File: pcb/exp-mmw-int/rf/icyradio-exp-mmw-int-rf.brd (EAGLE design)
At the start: 85.7 x 98.4 mm, 68 parts, among them U1 ADMV1013, U2 ADMV1014

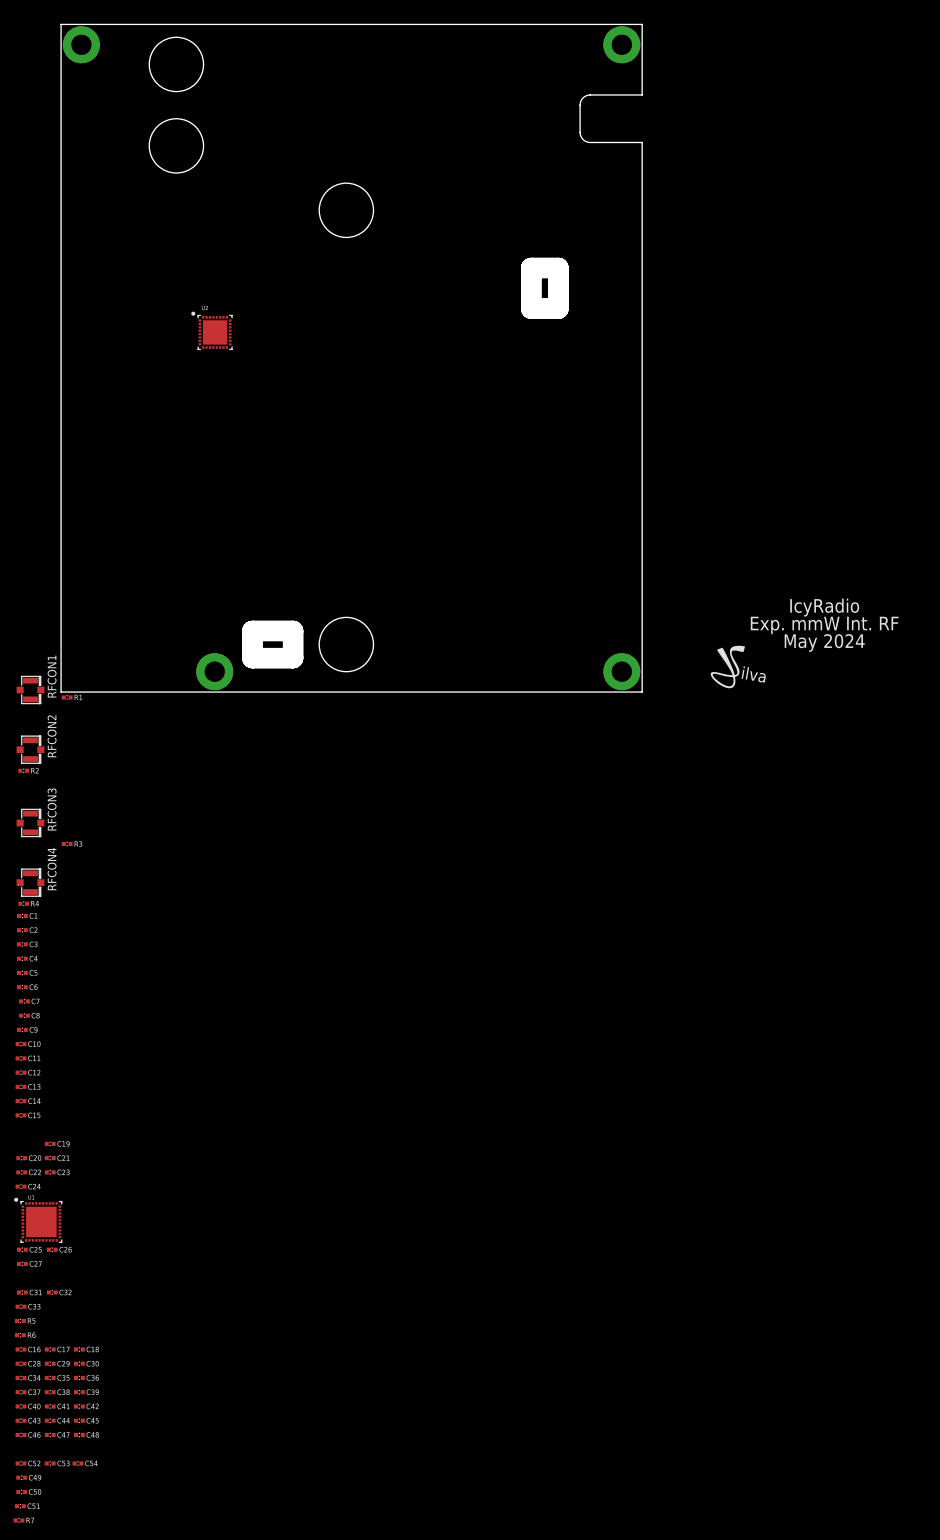
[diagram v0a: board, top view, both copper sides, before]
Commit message: pcb: Finish mmWave integrated expansion PCBs for production
Signed-off-by: João Silva <jgc3silva@gmail.com>
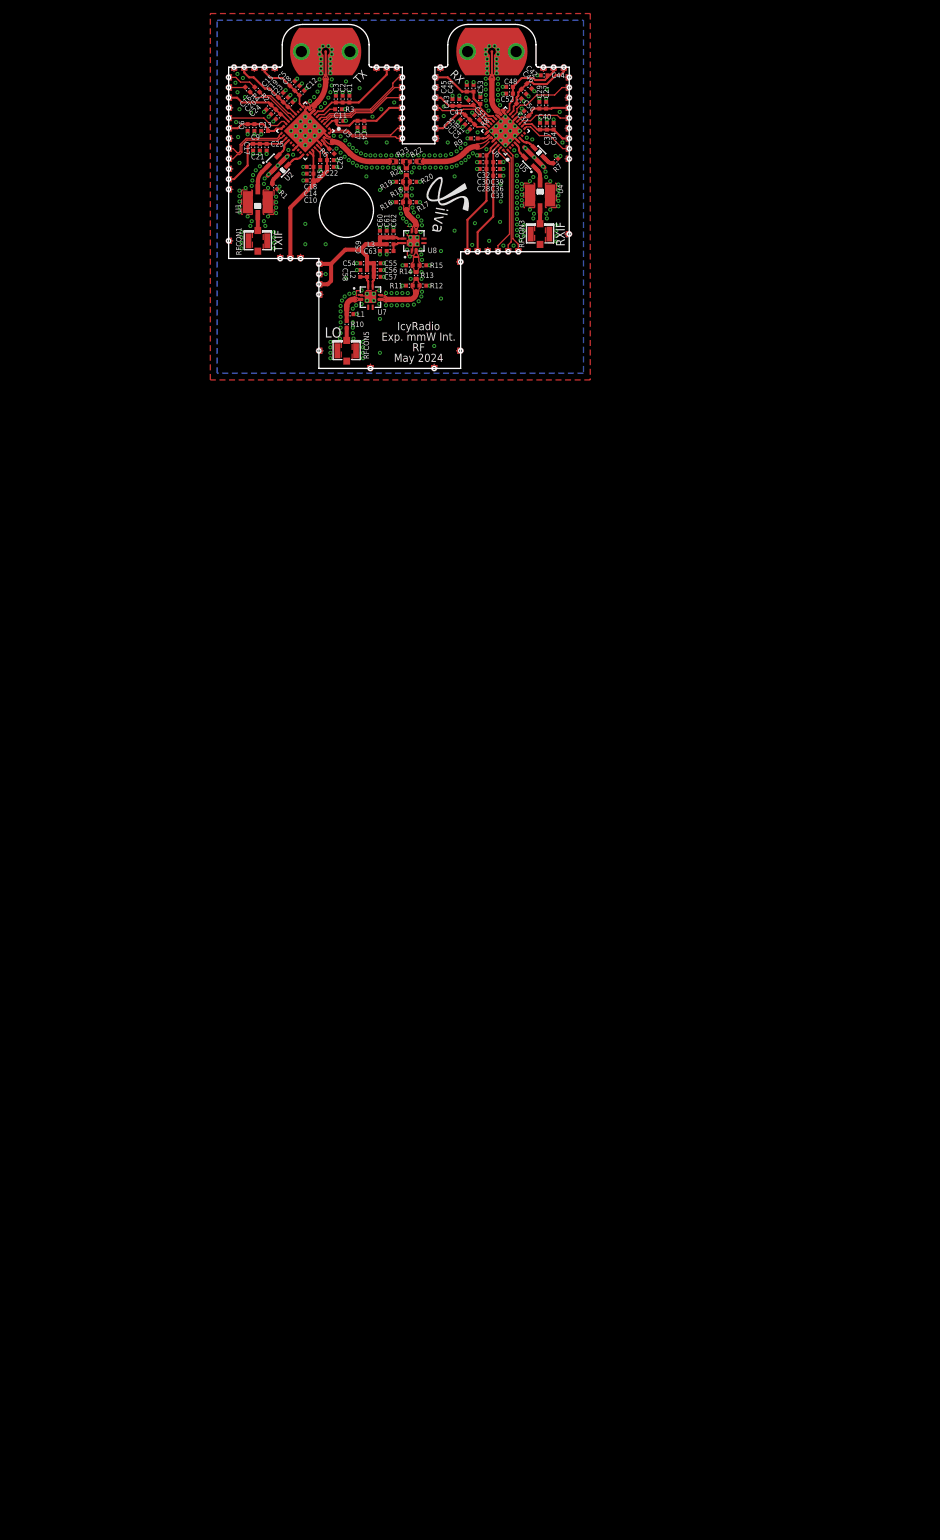
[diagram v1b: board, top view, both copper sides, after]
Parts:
- added C55, C60: 5.6pF, Capacitor:CAP0402
- added C56, C61: 18pF, Capacitor:CAP0402
- added C57, C62: 1nF, Capacitor:CAP0402
- added C58, C63: 100nF, Capacitor:CAP0402
- added C59: 10uF, Capacitor:CAP0402
- added L1: DNP, Inductor:IND0402
- added L2, L3: 3.3nH, Inductor:IND0402
- added P1, P10, P2, P22, P23, P24, P25, P26, P27, P28, P29, P3, P33, P34, P35, P36, P37, P38, P39, P4, P5, P52, P53, P54, P55, P56, P57, P58, P59, P6, P60, P64, P65, P7, P8, P9: CHOLE-0.9MM-SS, PADs:CAST_HOLE_0P9MM_SS
- added P11, P12, P13, P14, P15, P16, P17, P18, P19, P20, P21, P30, P31, P32, P40, P41, P42, P43, P44, P45, P46, P47, P48, P49, P50, P51, P61, P62, P63, P66, P67: CHOLE-0.9MM-DS, PADs:CAST_HOLE_0P9MM_DS
- added R10, R13, R18: 0 Ohms, Resistor:RES0402
- added R11, R12, R14, R15, R16, R17, R19, R20: DNP, Resistor:RES0402
- added R21, R22, R23: 16.7 Ohms, Resistor:RES0402
- added R8: 1.1K Ohms, Resistor:RES0402
- added R9: 50 Ohms, Resistor:RES0402
- added RFCON5: RFCON-U.FL, RF Connector:U.FL
- added U3: ADMV1013, Analog Devices:LGA40
- added U4: BFCV-2895+, Mini Circuits:JV1210C
- added U5: QCN-34+, Mini Circuits:FV1206-1
- added U6: ADMV1014, Analog Devices:LGA32
- added U7, U8: AVA-183A+, Mini Circuits:DQ849
- C11, C23, C26, C32, C41, C50, C53: value 10nF -> 100pF
- C13, C25, C31, C40, C52: value 10uF -> 100pF
- C15, C27, C33, C42, C45, C54, C6: value 100pF -> 10uF
- C17, C35, C44, C5: value 10nF -> 10uF
- C19, C22, C37, C46, C49, C7: value 10uF -> 10nF
- C21, C30, C36, C48, C9: value 100pF -> 10nF
- R1: value 0 Ohms -> 50 Ohms
- R2, R4: value 0 Ohms -> 1K Ohms
- R3: value 0 Ohms -> 1.1K Ohms
- R6, R7: value 1.1K Ohms -> 50 Ohms
- RFCON2, RFCON4: value RFCON-U.FL -> RFCON-HK-R-SR2-SA; device RF Connector:U.FL -> RF Connector:HK-R-SR2-SA
- U1: value ADMV1013 -> BFCV-2895+; device Analog Devices:LGA40 -> Mini Circuits:JV1210C
- U2: value ADMV1014 -> QCN-34+; device Analog Devices:LGA32 -> Mini Circuits:FV1206-1
- moved C50 217.7 mm to (67.5, 87.1), turned to 45 degrees
- moved C51 217.3 mm to (60.4, 86.9), turned to 135 degrees
- moved R7 215.4 mm to (72.9, 78.3), turned to 225 degrees
- moved C49 215.4 mm to (60.8, 89.0), turned to 90 degrees
- moved C52 214.4 mm to (66.1, 88.2), turned to 180 degrees
- moved C46 211.4 mm to (68.2, 88.5), turned to 315 degrees
- moved C44 211.2 mm to (71.2, 90.9), turned to 180 degrees
- moved C53 210.7 mm to (61.8, 87.2), turned to 90 degrees
- moved C48 208.6 mm to (66.1, 89.2), turned to 180 degrees
- moved C42 205.6 mm to (69.0, 89.3), turned to 315 degrees
- moved C47 205.4 mm to (58.7, 86.9), turned to 90 degrees
- moved C45 204.5 mm to (59.8, 89.0), turned to 90 degrees
- moved C43 204.4 mm to (57.7, 86.9), turned to 90 degrees
- moved C40 203.6 mm to (70.6, 83.4), turned to 90 degrees
- moved C37 202.1 mm to (71.6, 83.4), turned to 90 degrees
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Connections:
- removed net N$1: R1.2, RFCON1.P$3
- removed net N$2: R2.2, RFCON2.P$3
- removed net N$3: R3.2, RFCON3.P$3
- removed net N$4: R4.2, RFCON4.P$3
- removed net N$7: U1.30
- removed net N$8: U1.24
- removed net TX_BB_I_N: R2.1, U1.29
- removed net TX_BB_I_P: R1.1, U1.28
- removed net TX_BB_Q_N: R4.1, U1.25
- removed net TX_BB_Q_P: R3.1, U1.26
- new net 5V0_RF_LO: C54.1, C55.1, C56.1, C57.1, C59.1, C60.1, C61.1, C62.1, L2.1, L3.1, P64.PAD_T, P65.PAD_T, U7.7, U8.7
- new net LO_AMP1_IN: L1.1, R10.1, U7.2
- new net LO_AMP1_OUT: R11.2, R12.2, R13.2, U7.5
- new net LO_AMP2_IN: R13.1, R14.2, R15.2, U8.2
- new net LO_AMP2_OUT: R16.2, R17.2, R18.2, U8.5
- new net LO_AMP_VD1: C58.1, L2.2, U7.8
- new net LO_AMP_VD2: C63.1, L3.2, U8.8
- new net LO_IN: R10.2, RFCON5.P$3
- new net LO_OUT: R18.1, R19.2, R20.2, R21.2
- new net LO_SPLIT: R21.1, R22.2, R23.2
- new net N$11: R1.2, U2.3
- new net N$13: R7.2, U5.3
- new net N$17: R2.2, U3.15
- new net N$18: R4.2, U3.16
- new net RX_GAIN_VCTRL: P34.PAD_T, U6.14
- new net RX_IF: U4.1, U5.1
- new net RX_IF_FILT: RFCON3.P$3, U4.3
- new net RX_IF_I: U5.6, U6.4
- new net RX_IF_Q: U5.4, U6.6
- new net RX_LO: R22.1, U6.27
- new net RX_LO_N: R9.2, U6.26
- new net RX_PWR_VDET: P33.PAD_T, U6.11
- new net RX_RF: RFCON4.SIG, U6.18
- new net TX_GAIN_VCTRL1: P1.PAD_T, R2.1
- new net TX_GAIN_VCTRL2: P2.PAD_T, R4.1
- new net TX_IF_FILT: U1.3, U2.1
- new net TX_IF_I: U2.4, U3.30
- new net TX_IF_IN: RFCON1.P$3, U1.1
- new net TX_IF_Q: U2.6, U3.24
- new net TX_LO: R23.1, U3.38
- new net TX_LO_N: R6.2, U3.37
- new net TX_PWR_VDET_N: P4.PAD_T, U3.21
- new net TX_PWR_VDET_P: P3.PAD_T, U3.22
- new net TX_RF: RFCON2.SIG, U3.9
- net !RX_RST: now also P39.PAD_T, U6.22; no longer U2.22
- net !RX_SPI_SEN: now also P35.PAD_T, U6.1; no longer U2.1
- net !TX_RST: now also P10.PAD_T, U3.1; no longer U1.1
- net !TX_SPI_SEN: now also P6.PAD_T, U3.40; no longer U1.40
- net !TX_SPI_SEN2: now also P5.PAD_T, U3.18; no longer U1.18
- net 1V5_RF_RX: now also C45.1, C49.1, P52.PAD_T, U6.20; no longer C52.1, C54.1, U2.20
- net 1V8_RF_RX: now also C33.1, C36.1, C39.1, C42.1, C46.1, C50.1, P53.PAD_T, P54.PAD_T, U6.15, U6.30; no longer C16.1, C17.1, C18.1, C28.1, C29.1, C30.1, U2.15, U2.30
- net 1V8_RF_TX: now also C11.1, C15.1, C19.1, C23.1, C7.1, P22.PAD_T, P23.PAD_T, U3.14, U3.2; no longer C1.1, C2.1, C3.1, C5.1, C6.1, U1.14, U1.2
- net 3V3_RF_RX: now also C27.1, C28.1, C29.1, C30.1, C31.1, C32.1, C51.1, C52.1, P55.PAD_T, P56.PAD_T, P57.PAD_T, P58.PAD_T, P59.PAD_T, P60.PAD_T, U6.10, U6.12, U6.16, U6.21, U6.24, U6.29; no longer C36.1, C39.1, C42.1, C45.1, C46.1, U2.10, U2.12, U2.16, U2.21, U2.24, U2.29
- net 3V3_RF_TX: now also C1.1, C16.1, C17.1, C18.1, C2.1, C3.1, C5.1, C6.1, P24.PAD_T, P25.PAD_T, P26.PAD_T, P27.PAD_T, P28.PAD_T, P29.PAD_T, U3.11, U3.17, U3.19, U3.20, U3.23, U3.32, U3.33, U3.35, U3.7; no longer C11.1, C15.1, C19.1, C23.1, C27.1, C31.1, C32.1, C33.1, C7.1, U1.11, U1.17, U1.19, U1.20, U1.23, U1.32, U1.33, U1.35, U1.7
- net GND: now also C55.2, C56.2, C57.2, C58.2, C59.2, C60.2, C61.2, C62.2, C63.2, L1.2, P11.PAD_B, P11.PAD_T, P12.PAD_B, P12.PAD_T, P13.PAD_B, P13.PAD_T, P14.PAD_B, P14.PAD_T, P15.PAD_B, P15.PAD_T, P16.PAD_B, P16.PAD_T, P17.PAD_B, P17.PAD_T, P18.PAD_B, P18.PAD_T, P19.PAD_B, P19.PAD_T, P20.PAD_B, P20.PAD_T, P21.PAD_B, P21.PAD_T, P30.PAD_B, P30.PAD_T, P31.PAD_B, P31.PAD_T, P32.PAD_B, P32.PAD_T, P40.PAD_B, P40.PAD_T, P41.PAD_B, P41.PAD_T, P42.PAD_B, P42.PAD_T, P43.PAD_B, P43.PAD_T, P44.PAD_B, P44.PAD_T, P45.PAD_B, P45.PAD_T, P46.PAD_B, P46.PAD_T, P47.PAD_B, P47.PAD_T, P48.PAD_B, P48.PAD_T, P49.PAD_B, P49.PAD_T, P50.PAD_B, P50.PAD_T, P51.PAD_B, P51.PAD_T, P61.PAD_B, P61.PAD_T, P62.PAD_B, P62.PAD_T, P63.PAD_B, P63.PAD_T, P66.PAD_B, P66.PAD_T, P67.PAD_B, P67.PAD_T, R1.1, R11.1, R12.1, R14.1, R15.1, R16.1, R17.1, R19.1, R20.1, R3.1, R8.1, R9.1, RFCON2.GND@1, RFCON2.GND@2, RFCON4.GND@1, RFCON4.GND@2, RFCON5.P$1, RFCON5.P$2, U1.2, U1.4, U2.2, U3.10, U3.27, U3.36, U3.39, U3.41, U3.8, U4.2, U4.4, U5.2, U5.5, U6.13, U6.17, U6.19, U6.25, U6.28, U6.33, U6.5, U7.1, U7.6, U7.9, U8.1, U8.6, U8.9; no longer RFCON2.P$1, RFCON2.P$2, RFCON4.P$1, RFCON4.P$2, U1.10, U1.27, U1.36, U1.39, U1.41, U1.8, U2.13, U2.17, U2.19, U2.25, U2.28, U2.33
- net N$5: now also R3.2, U3.6; no longer R5.2, U1.6
- net N$6: now also R5.2, U3.34; no longer R6.2, U1.34
- net N$9: now also R8.2, U6.23; no longer R7.2, U2.23
- net RX_SPI_SCLK: now also P36.PAD_T, U6.31; no longer U2.31
- net RX_SPI_SDI: now also P38.PAD_T, U6.32; no longer U2.32
- net RX_SPI_SDO: now also P37.PAD_T, U6.9; no longer U2.9
- net TX_SPI_SCLK: now also P7.PAD_T, U3.3; no longer U1.3
- net TX_SPI_SDI: now also P9.PAD_T, U3.4; no longer U1.4
- net TX_SPI_SDO: now also P8.PAD_T, U3.5; no longer U1.5
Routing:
- net 3V3_RF_TX: track 0.00 -> 79.3 mm
- net 3V3_RF_RX: track 0.00 -> 64.6 mm
- net GND: track 0.00 -> 52.0 mm, vias 4 -> 432
- net 1V8_RF_RX: track 0.00 -> 29.1 mm
- net 5V0_RF_LO: track 0.00 -> 27.8 mm
- net 1V8_RF_TX: track 0.00 -> 23.6 mm
- net RX_SPI_SCLK: track 0.00 -> 16.6 mm
- net RX_SPI_SDI: track 0.00 -> 15.4 mm
- net !RX_SPI_SEN: track 0.00 -> 15.4 mm
- net TX_SPI_SDO: track 0.00 -> 14.8 mm
- net TX_SPI_SDI: track 0.00 -> 13.7 mm
- net TX_SPI_SCLK: track 0.00 -> 12.8 mm
- net 1V5_RF_RX: track 0.00 -> 12.2 mm
- net !TX_RST: track 0.00 -> 11.3 mm
- net !TX_SPI_SEN: track 0.00 -> 11.0 mm
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- added copper zone on layer 1, net GND
- added copper zone on layer 16, net GND
- added copper zone on layer 1, net LO_AMP1_IN
- added copper zone on layer 1, net LO_AMP1_OUT
- added copper zone on layer 1, net LO_AMP2_IN
- added copper zone on layer 1, net LO_AMP2_OUT
- added copper zone on layer 1, net LO_OUT
- added copper zone on layer 1, net LO_SPLIT
- added copper zone on layer 1, net RX_LO
- added copper zone on layer 1, net RX_RF
- added copper zone on layer 1, net TX_LO
- added copper zone on layer 1, net TX_RF
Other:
- board size 85.7 x 98.4 mm -> 50.2 x 50.7 mm
- board text added: "LO"
- board text added: "RX"
- board text added: "RXIF"
- board text added: "TX"
- board text added: "TXIF"
